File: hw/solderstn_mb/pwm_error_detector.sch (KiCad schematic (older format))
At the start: 14 parts, among them Q1501 DMG1013T, U1501 NE556, U1502 74LVC1G175, U1503 74LVC1G11

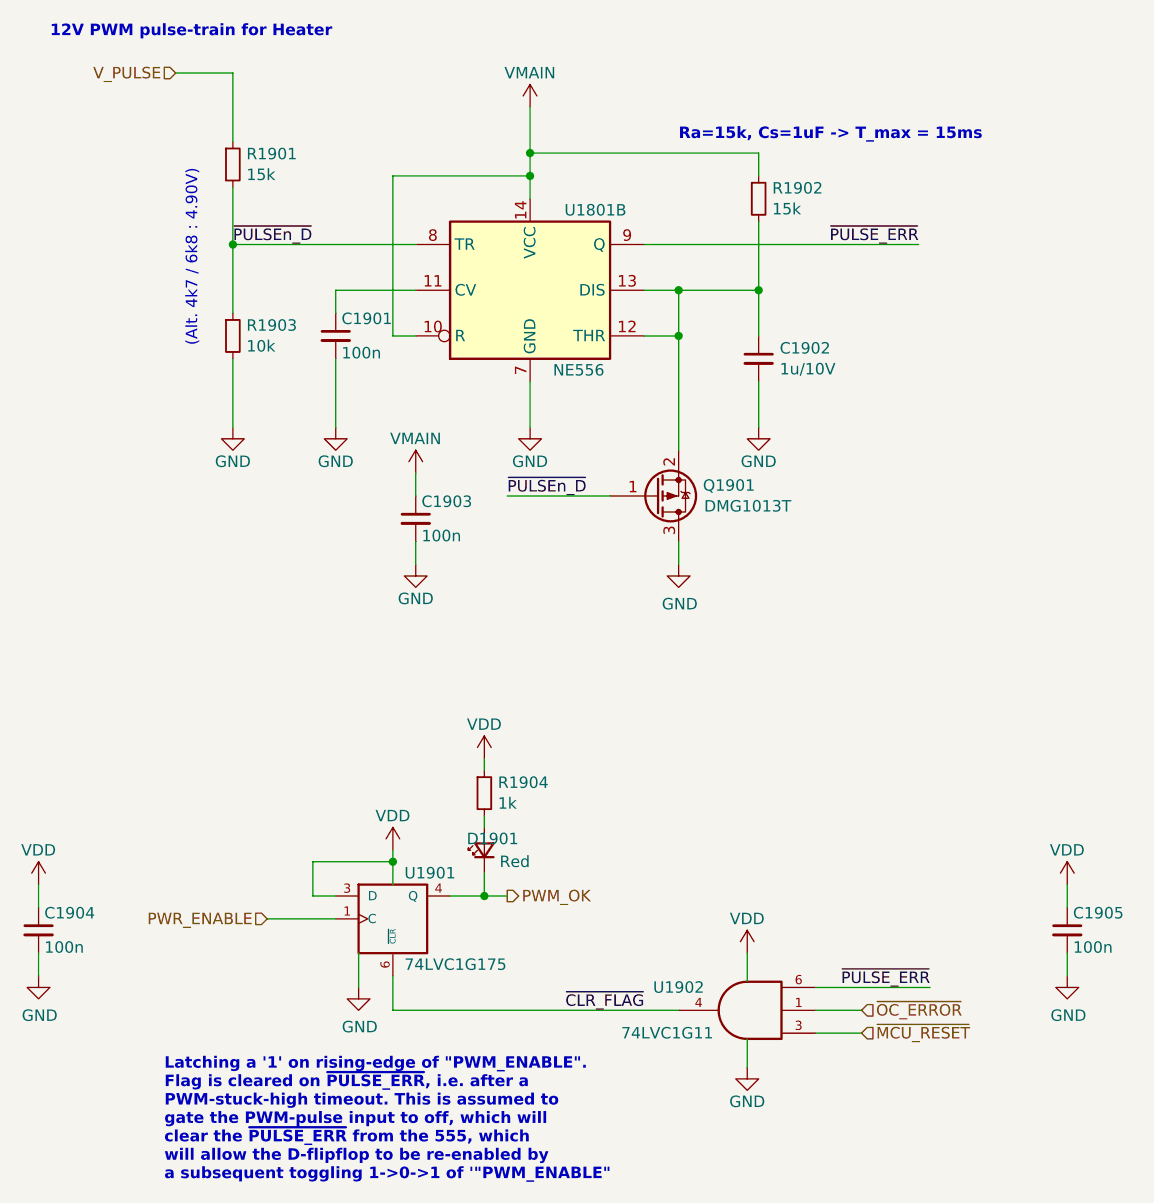
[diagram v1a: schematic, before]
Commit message: Updated display-board sch & PCB with optional left-hand rotary encoder instead of pwrbtn. Printed MB schematic updates PDF for 20-08-21
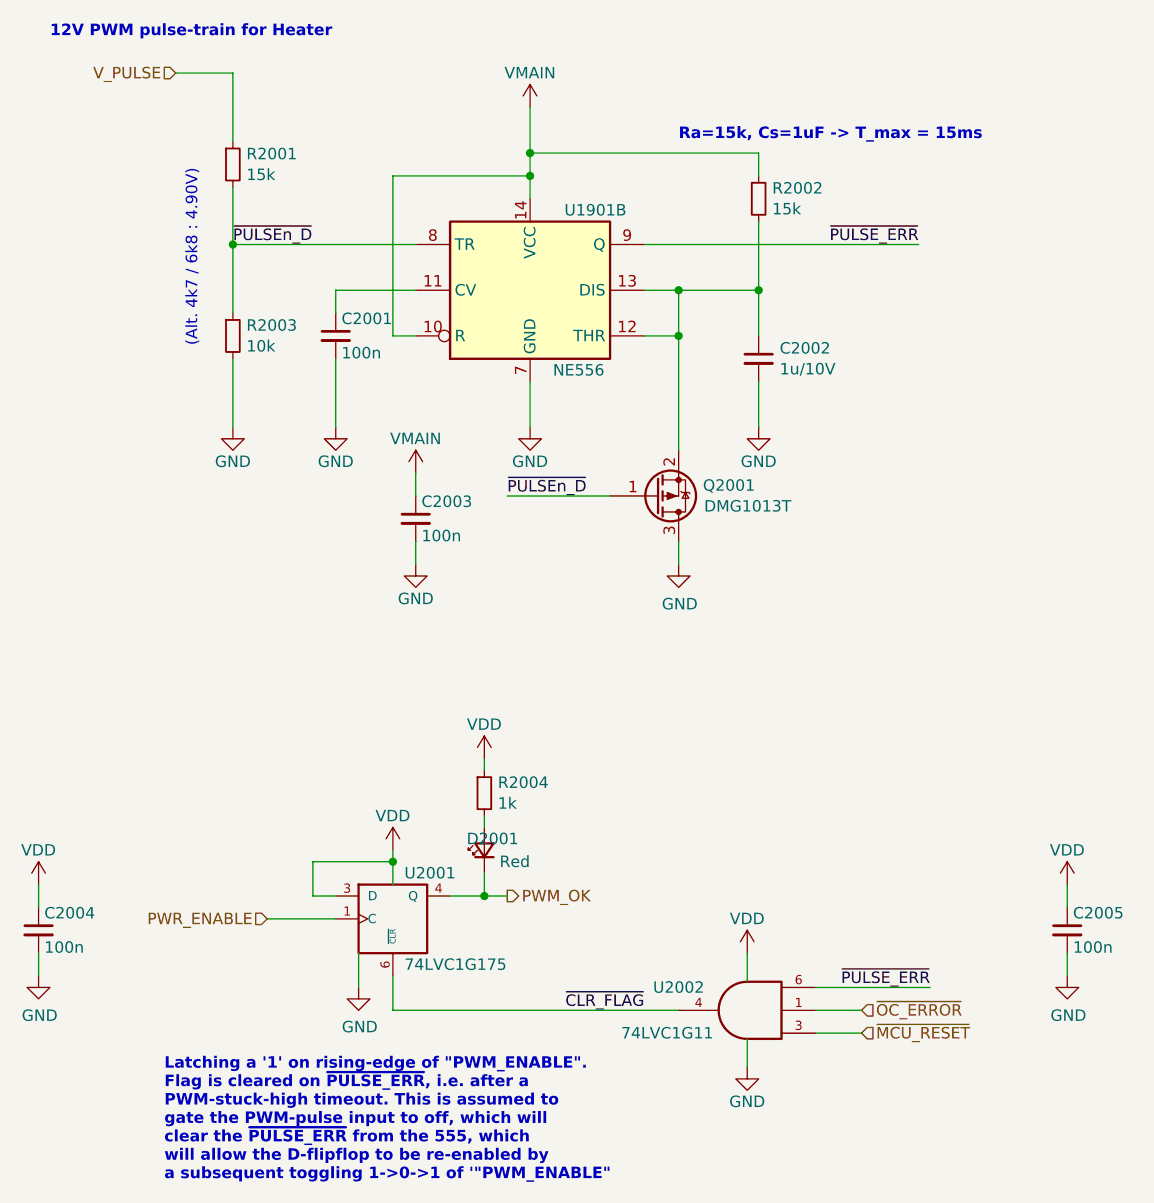
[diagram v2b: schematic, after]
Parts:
- renumbered C1501 to C1601, C1502 to C1602, C1503 to C1603, C1504 to C1604, C1505 to C1605, D1501 to D1601, Q1501 to Q1601, R1501 to R1601, R1502 to R1602, R1503 to R1603, R1504 to R1604, U1501 to U1601, U1502 to U1602, U1503 to U1603

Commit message: Corrected several ERC issues. Re-annotated & assigned all footprints except 32k xtal (will prob. replace with RTC module anyway)
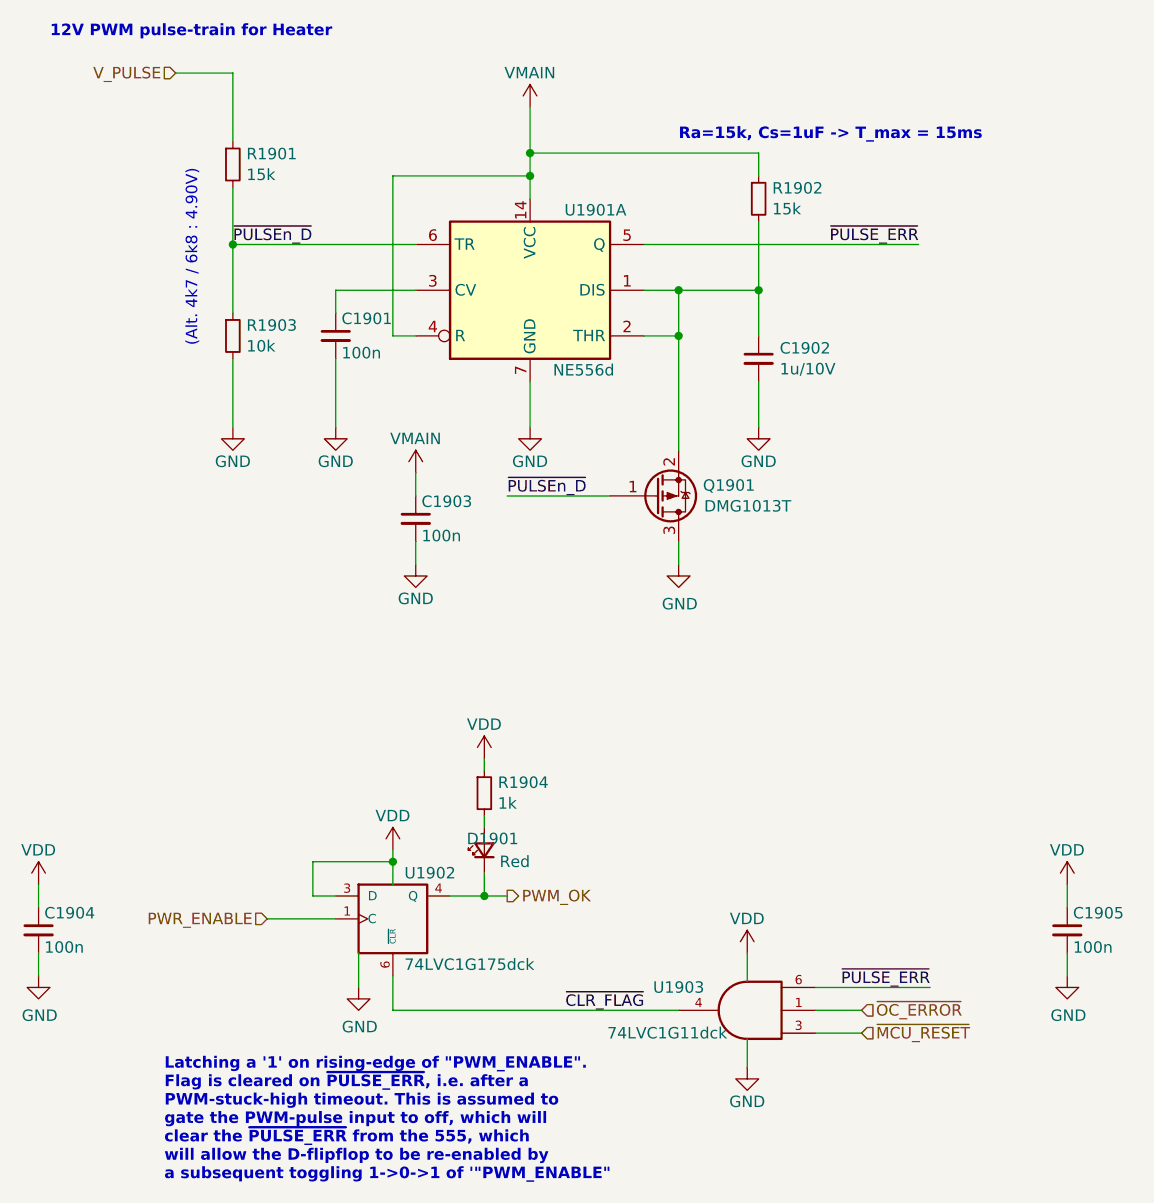
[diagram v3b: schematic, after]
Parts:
- C1601, C1602, C1603, C1604, C1605: footprint (none) -> Capacitor_SMD:C_0603_1608Metric
- D1601: footprint (none) -> LED_SMD:LED_0603_1608Metric
- Q1601: footprint bobs:SOT-523 -> customlib_mj_fp:SOT-523
- R1601, R1602, R1603, R1604: footprint (none) -> Resistor_SMD:R_0603_1608Metric
- U1601: value NE556 -> NE556d; footprint (none) -> Package_SO:SOIC-14_3.9x8.7mm_P1.27mm
- U1602: value 74LVC1G175 -> 74LVC1G175dck; footprint (none) -> Package_TO_SOT_SMD:SOT-363_SC-70-6_Handsoldering
- U1603: value 74LVC1G11 -> 74LVC1G11dck; footprint (none) -> Package_TO_SOT_SMD:SOT-363_SC-70-6_Handsoldering
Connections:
- net VMAIN: now also U1601.4 (R); no longer U1601.10 (R)
- net ~PULSE_ERR~: now also U1601.5 (Q); no longer U1601.9 (Q)
- net ~PULSEn_D~: now also U1601.6 (TR); no longer U1601.8 (TR)
- net at C1601.1: now also U1601.3 (CV); no longer U1601.11 (CV)
- net at C1602.1, Q1601.2 (S), R1602.2: now also U1601.1 (DIS), U1601.2 (THR); no longer U1601.12 (THR), U1601.13 (DIS)
